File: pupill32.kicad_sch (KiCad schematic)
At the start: 48 parts, among them J1 HeaderR, J2 HeaderL, J3 USB_PINS, J4 SWD_HEADER, SW1 RST_BTN, SW2 BOOT_BTN, U1 SRV05-4, U2 PY32F030F18P6, U3 CH340N, U4 AMS1117-3.3, Y1 32.768 kHz, Y2 12M

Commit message: project rename, part2
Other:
- note added: "PU(rple)PILL32 rev.A"
- note removed: "PYPILL32 rev.A"
- title: pypill32 - indie py32f030 evaluation board -> pupill32 - indie py32f030 evaluation board
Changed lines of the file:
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@@
 	(paper "A4")
 	(title_block
-		(title "pypill32 - indie py32f030 evaluation board")
+		(title "pupill32 - indie py32f030 evaluation board")
 		(rev "A")
 	)
@@
 		)
 	)
-	(text "PYPILL32 rev.A"
+	(text "PU(rple)PILL32 rev.A"
 		(exclude_from_sim no)
-		(at 218.186 169.926 0)
+		(at 224.536 169.926 0)
 		(effects
 			(font

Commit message: project rename, part3
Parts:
- SW1, SW2: footprint pypill32:SW-SMD_L6.0-W3.5-LS8.2 -> pupill32:SW-SMD_L6.0-W3.5-LS8.2
- U2: symbol pypill32:PY32F030F1xPx -> pupill32:PY32F030F1xPx
- USB1: footprint pypill32:USB-C-SMD_TYPE-C-6PIN-2MD-073 -> pupill32:USB-C-SMD_TYPE-C-6PIN-2MD-073; symbol pypill32:TYPE-C16PIN2MD(073) -> pupill32:TYPE-C16PIN2MD(073)

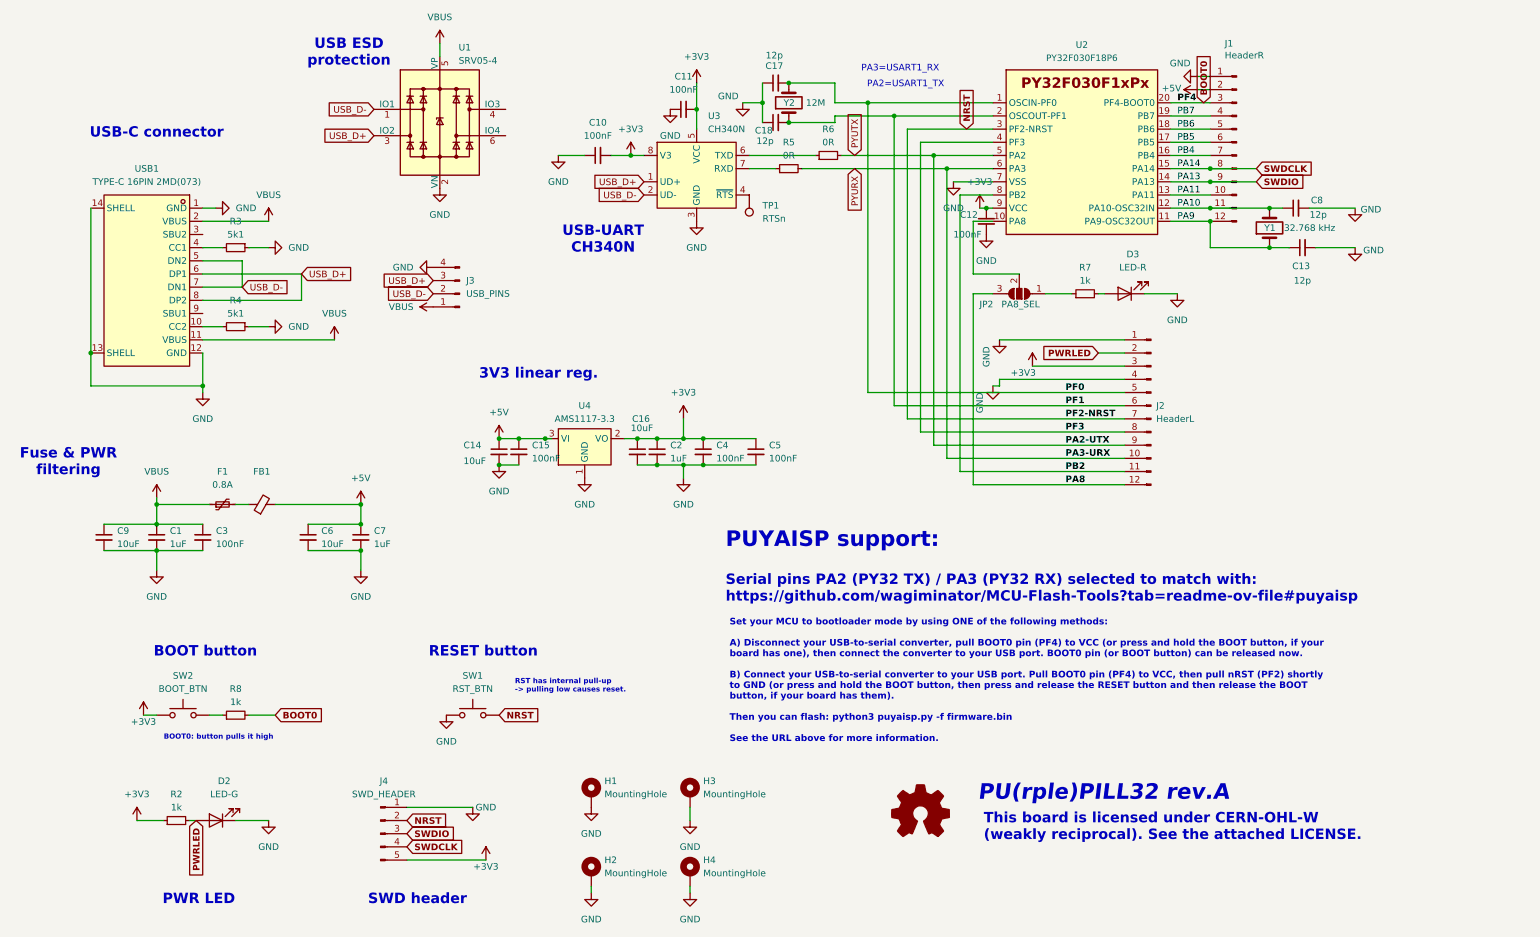
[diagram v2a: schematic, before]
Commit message: revA errata -> revB
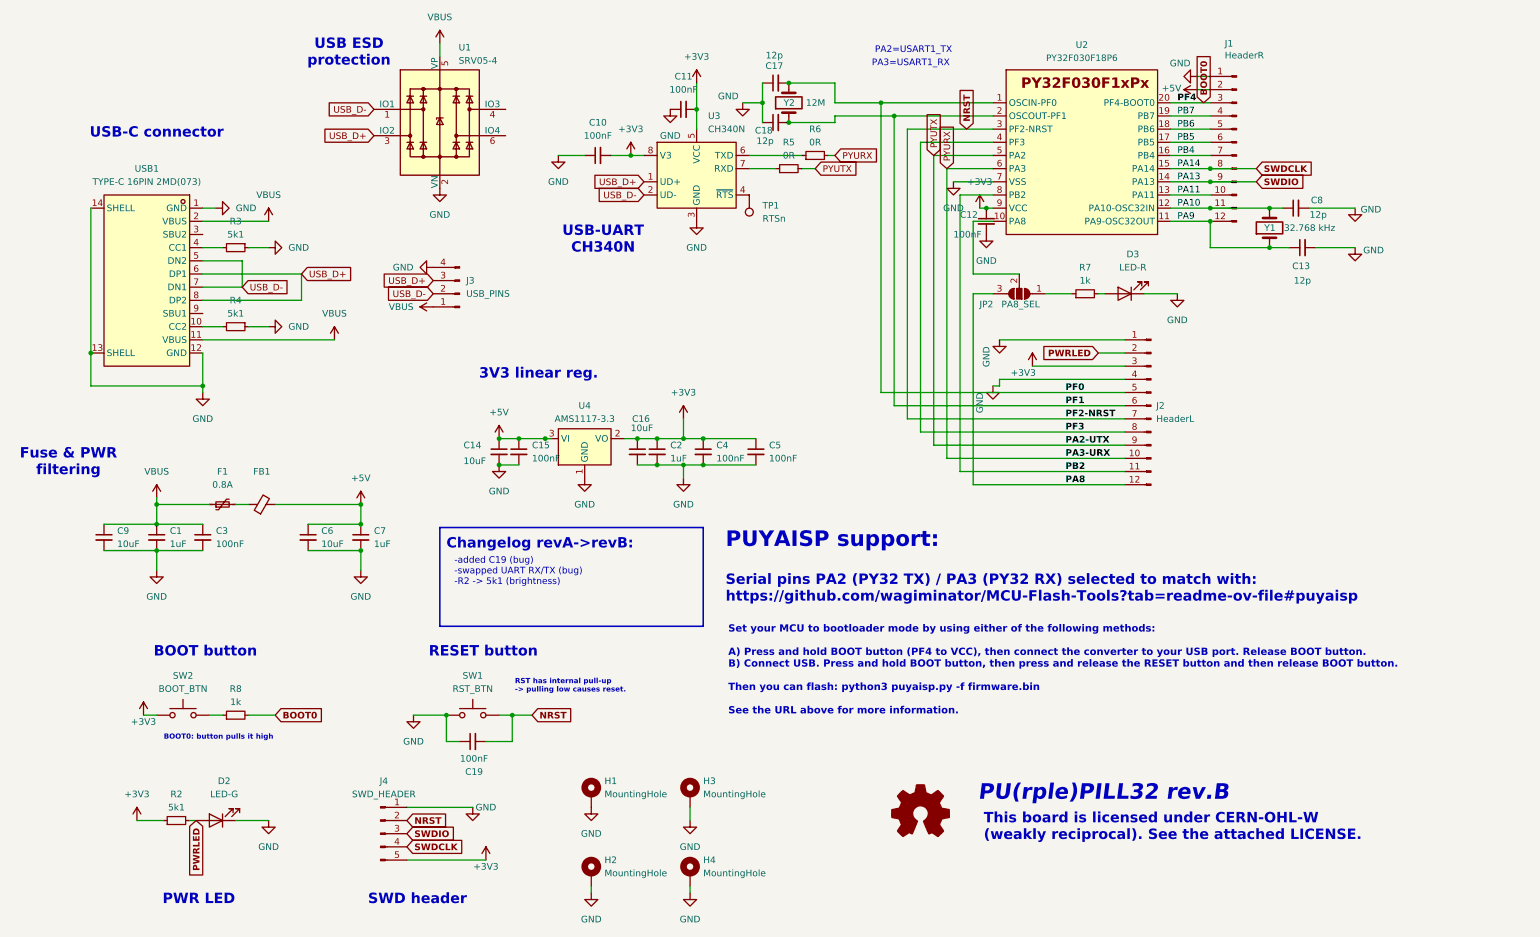
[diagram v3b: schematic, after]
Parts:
- added C19: 100nF, Capacitor_SMD:C_0805_2012Metric_Pad1.18x1.45mm_HandSolder, symbol Device:C_Small
- R2: value 1k -> 5k1
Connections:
- net GND: now also C19.1
- net NRST: now also C19.2
- net PYURX: now also R6.2; no longer R5.2
- net PYUTX: now also R5.2; no longer R6.2
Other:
- note added: "-added C19 (bug) -swapped UART RX/TX (bug) -R2 -> 5k1 (brightness)"
- note added: "Changelog revA->revB:"
- note added: "PU(rple)PILL32 rev.B"
- note added: "Set your MCU to bootloader mode by using either of the following methods: A) Press and hold BOOT button (PF4 to VCC), then connect the converter to your USB port. Release BOOT button. B) Connect USB. Press and hold BOOT button, then press and release the RESET button and then release BOOT button. Then you can flash: python3 puyaisp.py -f firmware.bin See the URL above for more information."
- note removed: "PU(rple)PILL32 rev.A"
- note removed: "Set your MCU to bootloader mode by using ONE of the following methods: A) Disconnect your USB-to-serial converter, pull BOOT0 pin (PF4) to VCC (or press and hold the BOOT button, if your board has one), then connect the converter to your USB port. BOOT0 pin (or BOOT button) can be released now. B) Connect your USB-to-serial converter to your USB port. Pull BOOT0 pin (PF4) to VCC, then pull nRST (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"
- moved on the sheet: R6

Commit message: schema update (stylish changes, no content changes)
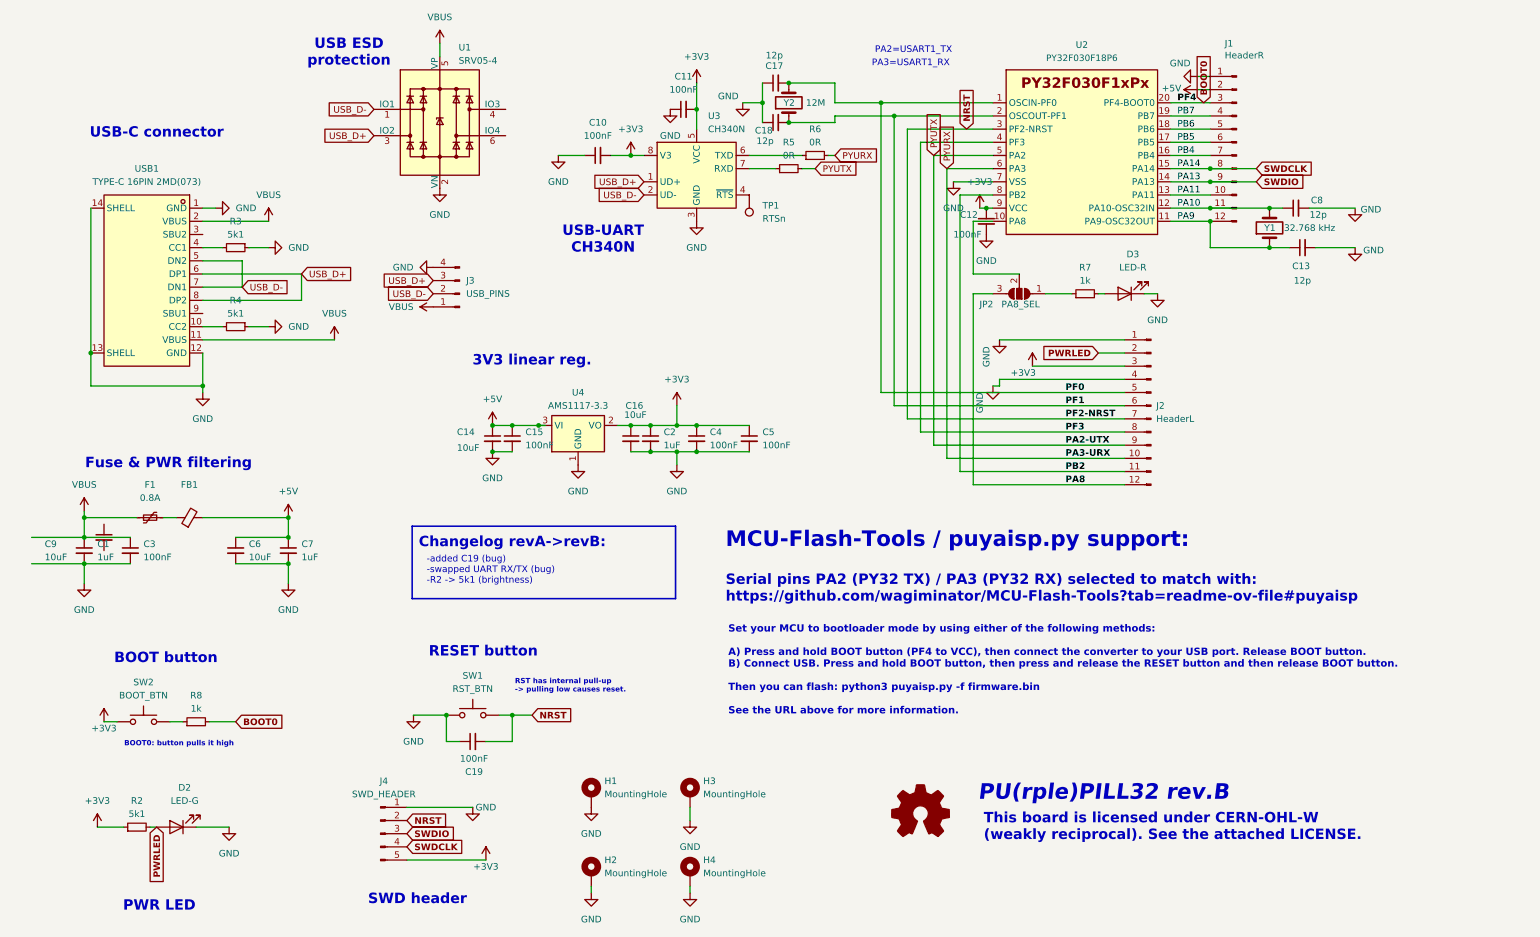
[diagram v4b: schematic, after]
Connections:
- net GND: no longer C9.2
- net VBUS: no longer C9.1
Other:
- note added: "MCU-Flash-Tools / puyaisp.py support:"
- note removed: "PUYAISP support:"
- moved on the sheet: C1, C14, C15, C16, C2, C3, C4, C5, C6, C7, D2, F1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

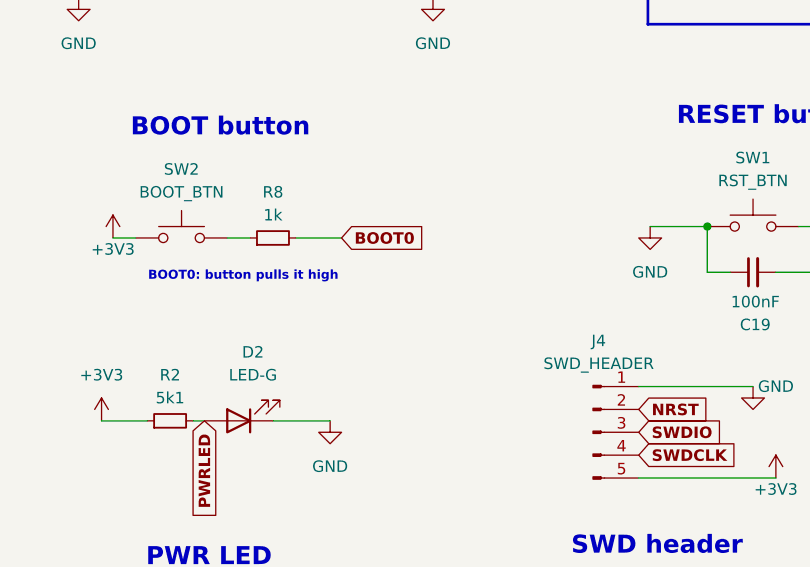
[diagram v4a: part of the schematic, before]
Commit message: R1 boot0 pulldown
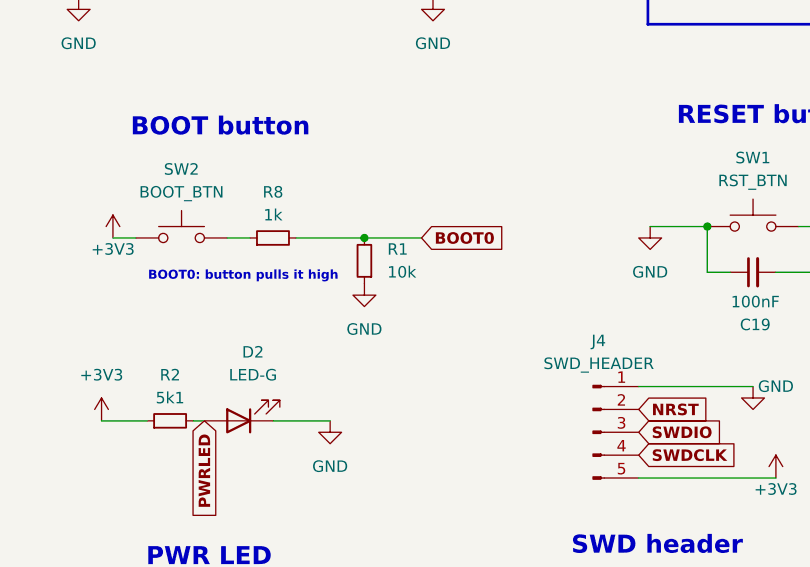
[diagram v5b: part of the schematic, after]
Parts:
- added R1: 10k, Resistor_SMD:R_0805_2012Metric_Pad1.20x1.40mm_HandSolder, symbol Device:R_Small
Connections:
- net BOOT0: now also R1.2
- net GND: now also R1.1
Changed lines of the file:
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@@
 	)
 	(junction
+		(at 59.69 156.21)
+		(diameter 0)
+		(color 0 0 0 0)
+	)
+	(junction
 		(at 50.8 91.44)
 		(diameter 0)
@@
 	(wire
 		(pts
+			(xy 59.69 156.21) (xy 66.04 156.21)
+		)
+		(stroke
+			(width 0)
+			(type default)
+		)
+	)
+	(wire
+		(pts
 			(xy 57.15 125.73) (xy 67.31 125.73)
 		)
@@
 	(wire
 		(pts
-			(xy 52.07 156.21) (xy 57.15 156.21)
+			(xy 52.07 156.21) (xy 59.69 156.21)
 		)
 		(stroke
@@
 	(global_label "BOOT0"
 		(shape input)
-		(at 57.15 156.21 0)
+		(at 66.04 156.21 0)
 		(fields_autoplaced yes)
 		(effects
@@
 		)
 		(property "Intersheetrefs" "${INTERSHEET_REFS}"
-			(at 66.7193 156.21 0)
+			(at 75.6093 156.21 0)
 			(effects
 				(font
@@
 	)
 	(symbol
+		(lib_id "power:GND")
+		(at 59.69 161.29 0)
+		(unit 1)
+		(exclude_from_sim no)
+		(in_bom yes)
+		(on_board yes)
+		(dnp no)
+		(fields_autoplaced yes)
+		(property "Reference" "#PWR020"
+			(at 59.69 167.64 0)
+			(effects
+				(font
+					(size 1.27 1.27)
+				)
+				(hide yes)
+			)
+		)
+		(property "Value" "GND"
+			(at 59.69 166.37 0)
+			(effects
+				(font
+					(size 1.27 1.27)
+				)
+			)
+		)
+		(property "Footprint" ""
+			(at 59.69 161.29 0)
+			(effects
+				(font
+					(size 1.27 1.27)
+				)
+				(hide yes)
+			)
+		)
+		(property "Datasheet" ""
+			(at 59.69 161.29 0)
+			(effects
+				(font
+					(size 1.27 1.27)
+				)
+				(hide yes)
+			)
+		)
+		(property "Description" ""
+			(at 59.69 161.29 0)
+			(effects
+				(font
+					(size 1.27 1.27)
+				)
+				(hide yes)
+			)
+		)
+		(pin "1"
+		)
+		(instances
+			(project "pupill32"
+				(path "/0471bd21-091d-469f-a793-0e3efa813f7b"
+					(reference "#PWR020")
+					(unit 1)
+				)
+			)
+		)
+	)
+	(symbol
 		(lib_id "Device:R_Small")
 		(at 57.15 64.77 270)
@@
 					(unit 1)
 				)
+			)
+		)
+	)
+	(symbol
+		(lib_id "Device:R_Small")
+		(at 59.69 158.75 180)
+		(unit 1)
+		(exclude_from_sim no)
+		(in_bom yes)
+		(on_board yes)
+		(dnp no)
+		(fields_autoplaced yes)
+		(property "Reference" "R1"
+			(at 62.23 157.4799 0)
+			(effects
+				(font
+					(size 1.27 1.27)
+				)
+				(justify right)
+			)
+		)
+		(property "Value" "10k"
+			(at 62.23 160.0199 0)
+			(effects
+				(font
+					(size 1.27 1.27)
+				)
+				(justify right)
+			)
+		)
+		(property "Footprint" "Resistor_SMD:R_0805_2012Metric_Pad1.20x1.40mm_HandSolder"
+			(at 59.69 158.75 0)
+			(effects
+				(font
+					(size 1.27 1.27)
+				)
+				(hide yes)
+			)
+		)
+		(property "Datasheet" "~"
+			(at 59.69 158.75 0)
+			(effects
+				(font
+					(size 1.27 1.27)
+				)
+				(hide yes)
+			)
+		)
+		(property "Description" ""
+			(at 59.69 158.75 0)
+			(effects
+				(font
+					(size 1.27 1.27)
+				)
+				(hide yes)
+			)
+		)
+		(pin "2"
+		)
+		(pin "1"
+		)
+		(instances
+			(project "pupill32"
+				(path "/0471bd21-091d-469f-a793-0e3efa813f7b"
+					(reference "R1")
+					(unit 1)
+				)

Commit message: schema changelog update
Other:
- note added: "-added C19 (bug) -swapped UART RX/TX (bug) -R2 -> 5k1 (brightness) -added R1 (BOOT0 pulldown)"
- note removed: "-added C19 (bug) -swapped UART RX/TX (bug) -R2 -> 5k1 (brightness)"
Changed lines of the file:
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@@
 		)
 	)
-	(text "-added C19 (bug)\n-swapped UART RX/TX (bug)\n-R2 -> 5k1 (brightness)"
+	(text "-added C19 (bug)\n-swapped UART RX/TX (bug)\n-R2 -> 5k1 (brightness)\n-added R1 (BOOT0 pulldown)"
 		(exclude_from_sim no)
-		(at 93.98 127 0)
+		(at 93.98 128.016 0)
 		(effects
 			(font

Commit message: tantalum
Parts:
- removed C16: 10uF, Capacitor_SMD:C_0805_2012Metric_Pad1.18x1.45mm_HandSolder, symbol Device:C_Small
- removed C2: 1uF, Capacitor_SMD:C_0805_2012Metric_Pad1.18x1.45mm_HandSolder, symbol Device:C_Small
- added C20: 22uF, Capacitor_Tantalum_SMD:CP_EIA-3528-21_Kemet-B_Pad1.50x2.35mm_HandSolder, symbol Device:C_Polarized_Small
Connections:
- net +3V3: now also C20.1
- net GND: now also C20.2
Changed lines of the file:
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@@
 	)
 	(junction
-		(at 137.16 104.14)
-		(diameter 0)
-		(color 0 0 0 0)
-	)
-	(junction
 		(at 245.11 52.07)
 		(diameter 0)
@@
 	)
 	(junction
-		(at 137.16 99.06)
-		(diameter 0)
-		(color 0 0 0 0)
-	)
-	(junction
 		(at 245.11 59.69)
 		(diameter 0)
@@
 	)
 	(junction
+		(at 133.35 99.06)
+		(diameter 0)
+		(color 0 0 0 0)
+	)
+	(junction
 		(at 110.49 99.06)
 		(diameter 0)
@@
 	)
 	(junction
-		(at 133.35 99.06)
-		(diameter 0)
-		(color 0 0 0 0)
-	)
-	(junction
 		(at 142.24 104.14)
 		(diameter 0)
@@
 	(wire
 		(pts
-			(xy 133.35 104.14) (xy 137.16 104.14)
-		)
-		(stroke
-			(width 0)
-			(type default)
-		)
-	)
-	(wire
-		(pts
 			(xy 29.21 57.15) (xy 29.21 85.09)
 		)
@@
 	(wire
 		(pts
-			(xy 137.16 104.14) (xy 142.24 104.14)
+			(xy 133.35 104.14) (xy 142.24 104.14)
 		)
 		(stroke
@@
 	(wire
 		(pts
-			(xy 133.35 99.06) (xy 137.16 99.06)
+			(xy 130.81 99.06) (xy 133.35 99.06)
 		)
 		(stroke
@@
 	(wire
 		(pts
-			(xy 130.81 99.06) (xy 133.35 99.06)
-		)
-		(stroke
-			(width 0)
-			(type default)
-		)
-	)
-	(wire
-		(pts
 			(xy 125.73 189.23) (xy 125.73 187.96)
 		)
@@
 	(wire
 		(pts
-			(xy 137.16 99.06) (xy 142.24 99.06)
+			(xy 133.35 99.06) (xy 142.24 99.06)
 		)
 		(stroke
@@
 	)
 	(symbol
-		(lib_id "Device:C_Small")
-		(at 133.35 101.6 0)
-		(unit 1)
-		(exclude_from_sim no)
-		(in_bom yes)
-		(on_board yes)
-		(dnp no)
-		(property "Reference" "C16"
-			(at 132.334 95.25 0)
-			(effects
-				(font
-					(size 1.27 1.27)
-				)
-				(justify left)
-			)
-		)
-		(property "Value" "10uF"
-			(at 132.08 97.028 0)
-			(effects
-				(font
-					(size 1.27 1.27)
-				)
-				(justify left)
-			)
-		)
-		(property "Footprint" "Capacitor_SMD:C_0805_2012Metric_Pad1.18x1.45mm_HandSolder"
-			(at 133.35 101.6 0)
-			(effects
-				(font
-					(size 1.27 1.27)
-				)
-				(hide yes)
-			)
-		)
-		(property "Datasheet" "~"
-			(at 133.35 101.6 0)
-			(effects
-				(font
-					(size 1.27 1.27)
-				)
-				(hide yes)
-			)
-		)
-		(property "Description" ""
-			(at 133.35 101.6 0)
-			(effects
-				(font
-					(size 1.27 1.27)
-				)
-				(hide yes)
-			)
-		)
-		(pin "1"
-		)
-		(pin "2"
-		)
-		(instances
-			(project "pupill32"
-				(path "/0471bd21-091d-469f-a793-0e3efa813f7b"
-					(reference "C16")
-					(unit 1)
-				)
-			)
-		)
-	)
-	(symbol
 		(lib_id "power:+3V3")
 		(at 146.05 33.02 0)
@@
 	)
 	(symbol
+		(lib_id "Device:C_Polarized_Small")
+		(at 133.35 101.6 0)
+		(unit 1)
+		(exclude_from_sim no)
+		(in_bom yes)
+		(on_board yes)
+		(dnp no)
+		(property "Reference" "C20"
+			(at 135.89 99.7838 0)
+			(effects
+				(font
+					(size 1.27 1.27)
+				)
+				(justify left)
+			)
+		)
+		(property "Value" "22uF"
+			(at 135.89 102.3238 0)
+			(effects
+				(font
+					(size 1.27 1.27)
+				)
+				(justify left)
+			)
+		)
+		(property "Footprint" "Capacitor_Tantalum_SMD:CP_EIA-3528-21_Kemet-B_Pad1.50x2.35mm_HandSolder"
+			(at 133.35 101.6 0)
+			(effects
+				(font
+					(size 1.27 1.27)
+				)
+				(hide yes)
+			)
+		)
+		(property "Datasheet" "~"
+			(at 133.35 101.6 0)
+			(effects
+				(font
+					(size 1.27 1.27)
+				)
+				(hide yes)
+			)
+		)
+		(property "Description" "Polarized capacitor, small symbol"
+			(at 133.35 101.6 0)
+			(effects
+				(font
+					(size 1.27 1.27)
+				)
+				(hide yes)
+			)
+		)
+		(property "TYPE" "Tantalum"
+			(at 134.366 105.41 0)
+			(effects
+				(font
+					(size 1.27 1.27)
+				)
+			)
+		)
+		(pin "2"
+		)
+		(pin "1"
+		)
+		(instances
+			(project ""
+				(path "/0471bd21-091d-469f-a793-0e3efa813f7b"
+					(reference "C20")
+					(unit 1)
+				)
+			)
+		)
+	)
+	(symbol
 		(lib_id "Mechanical:MountingHole_Pad")
 		(at 144.78 185.42 0)
@@
 					(unit 1)
 				)
-			)
-		)
-	)
-	(symbol
-		(lib_id "Device:C_Small")
-		(at 137.16 101.6 0)
-		(unit 1)
-		(exclude_from_sim no)
-		(in_bom yes)
-		(on_board yes)
-		(dnp no)
-		(fields_autoplaced yes)
-		(property "Reference" "C2"
-			(at 139.7 100.3363 0)
-			(effects
-				(font
-					(size 1.27 1.27)
-				)
-				(justify left)
-			)
-		)
-		(property "Value" "1uF"
-			(at 139.7 102.8763 0)
-			(effects
-				(font
-					(size 1.27 1.27)
-				)
-				(justify left)
-			)
-		)
-		(property "Footprint" "Capacitor_SMD:C_0805_2012Metric_Pad1.18x1.45mm_HandSolder"
-			(at 137.16 101.6 0)
-			(effects
-				(font
-					(size 1.27 1.27)
-				)
-				(hide yes)
-			)
-		)
-		(property "Datasheet" "~"
-			(at 137.16 101.6 0)
-			(effects
-				(font
-					(size 1.27 1.27)
-				)
-				(hide yes)
-			)
-		)
-		(property "Description" ""
-			(at 137.16 101.6 0)
-			(effects
-				(font
-					(size 1.27 1.27)
-				)
-				(hide yes)
-			)
-		)
-		(pin "1"
-		)
-		(pin "2"
-		)
-		(instances
-			(project "pupill32"
-				(path "/0471bd21-091d-469f-a793-0e3efa813f7b"
-					(reference "C2")
-					(unit 1)
-				)
